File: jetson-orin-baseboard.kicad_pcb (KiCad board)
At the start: 8 copper layers, 110 x 55 mm, 223 parts, among them J1 ERF8-040-05.0-L-DV-K-TR, J2 46756-1001, J301 1-2199230-6, J302 2199230-6, J401 USB4105-GF-A, J402 WE_632723300011_alt_symbol, J501 WE_632723300011_alt_symbol, J601 5-2337992-8, J701 WE_68715014522, J702 WE_68715014522, J801 TC2050-IDC-NL, M1 M2_4222, M2 jetson-orin-nx/nano-module, M301 M2_2280, Q401 BSS138W-7-F, Q402 BSS138W-7-F, Q701 BSS138W-7-F, Q702 BSS138W-7-F, Q703 BSS138W-7-F, Q704 BSS138W-7-F, Q802 BSS138W-7-F, Q901 BSS138W-7-F, SW901 PCM12SMTR, U401 RB521S30T1G, U402 TPS65988, U403 W25Q80DVUXIE_TR, U405 FT230XQ-R, U406 TPS7B8133DRVR, U407 TUSB1046-DCI, U410 TPD4E05U06QDQARQ1, U412 TPD4E05U06QDQARQ1, U501 HD3SS3220, U602 ULS-12/5-D48N-C, U701 PCA9547BS, U702 AP22615, U703 AP22615, U704 NX3DV642, U705 NX3DV642, U706 AP22615, U707 AP22615, U803 PCAL6416AHF, U901 RB521S30T1G, U902 RB521S30T1G, U903 MP2386GG-P, U904 MP2386GG-P

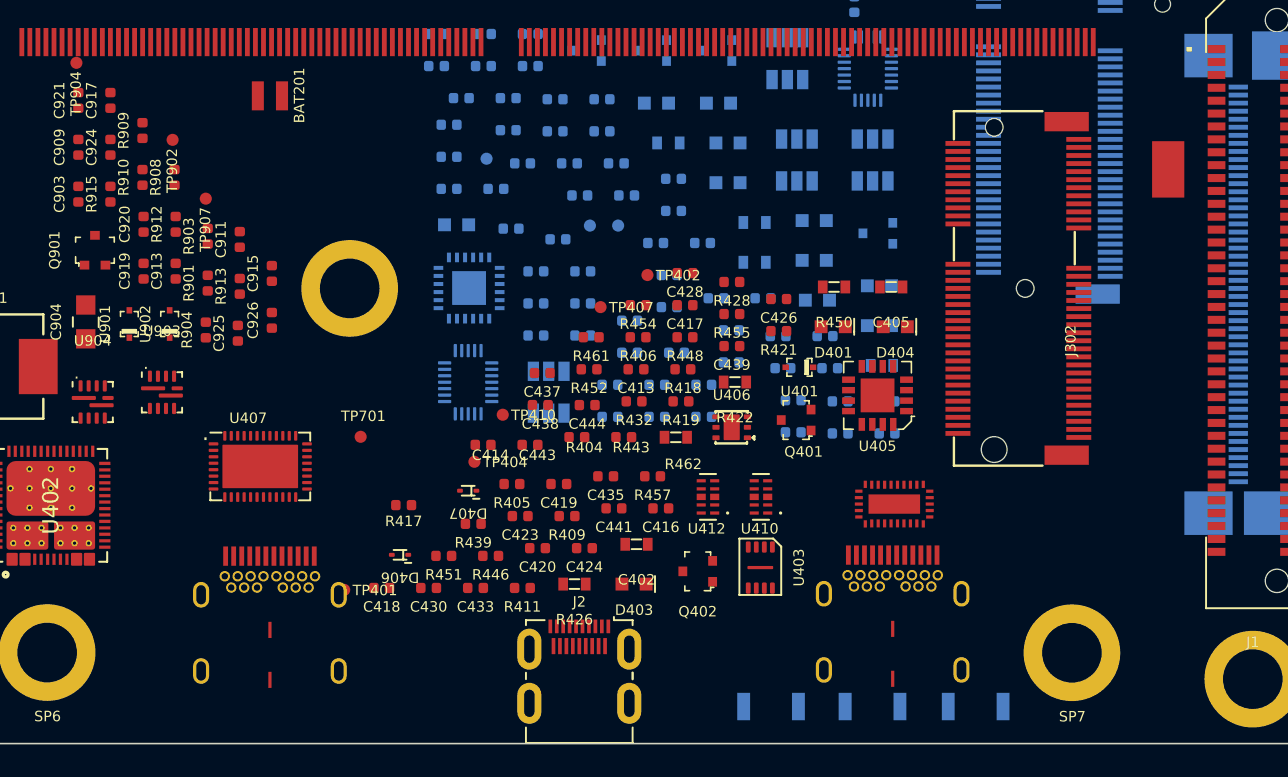
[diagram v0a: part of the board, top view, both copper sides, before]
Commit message: Update positions of the diodes
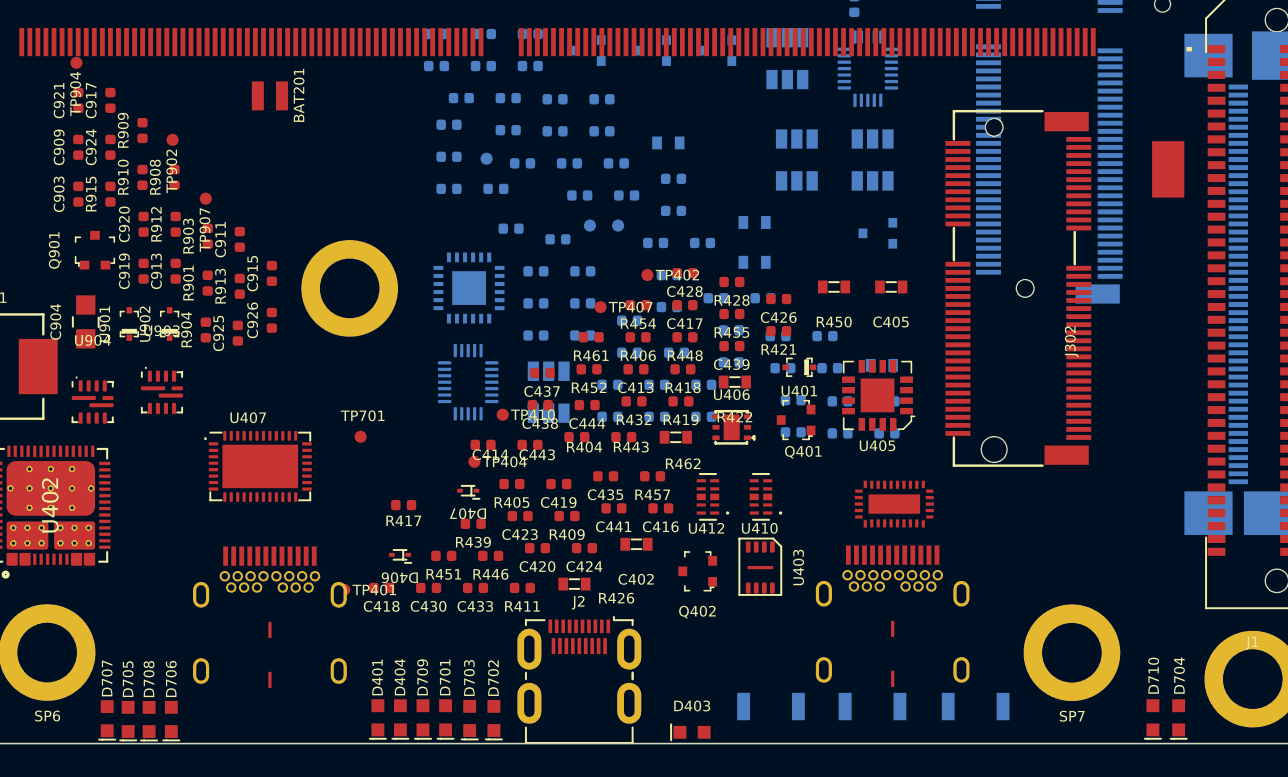
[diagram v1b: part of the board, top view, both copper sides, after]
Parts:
- D701, D702, D703, D704, D705, D706, D707, D708, D709, D710: moved to F.Cu
- moved D705 53.8 mm to (66.2, 123.5), turned to 90 degrees
- moved D706 50.3 mm to (68.9, 123.5), turned to 90 degrees
- moved D708 49.0 mm to (67.5, 123.5), turned to 90 degrees
- moved D701 41.7 mm to (85.9, 123.4), turned to 90 degrees
- moved D709 40.8 mm to (84.5, 123.4), turned to 90 degrees
- moved D703 39.2 mm to (87.4, 123.4), turned to 90 degrees
- moved D404 39.1 mm to (83.1, 123.4), turned to 90 degrees
- moved D707 37.5 mm to (64.9, 123.5), turned to 90 degrees
- moved D710 37.3 mm to (129.8, 123.4), turned to 90 degrees
- moved D401 37.3 mm to (81.7, 123.4), turned to 90 degrees
- moved D704 36.3 mm to (131.4, 123.4), turned to 90 degrees
- moved D702 36.3 mm to (88.9, 123.4), turned to 90 degrees
- moved D403 9.88 mm to (101.2, 124.3), turned to 0 degrees

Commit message: Import recently added components to PCB
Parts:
- removed the M1 at (124.8, 119.4)
- added A201: Jetson-Orin-9.2H-socket, antmicro-footprints:TE_2309413, F.Cu at (89.5, 77.4)
- added C1: C_1u_0402, antmicro-footprints:0402-cap, F.Cu at (-176.0, 142.6)
- added C10: C_100n_0402_50V, antmicro-footprints:0402-cap, F.Cu at (-168.9, 161.5)
- added C11: C_100n_0402, antmicro-footprints:0402-cap, F.Cu at (-151.4, 161.5)
- added C12: C_1u_0402, antmicro-footprints:0402-cap, F.Cu at (-168.2, 127.7)
- added C13: C_1u_0402, antmicro-footprints:0402-cap, F.Cu at (-185.8, 146.8)
- added C14: C_1u_0402, antmicro-footprints:0402-cap, F.Cu at (-163.5, 131.6)
- added C15: C_1u_0402, antmicro-footprints:0402-cap, F.Cu at (-180.0, 146.8)
- added C16: C_10u_25V_0603, antmicro-footprints:0603-cap, F.Cu at (-72.2, 116.4)
- added C17: C_10u_0402, antmicro-footprints:0402-cap, F.Cu at (-81.0, 130.0)
- added C18: C_100n_0402, antmicro-footprints:0402-cap, F.Cu at (-89.7, 92.7)
- added C19: C_100n_0402, antmicro-footprints:0402-cap, F.Cu at (-89.7, 90.8)
- added C2: C_100n_0402, antmicro-footprints:0402-cap, F.Cu at (-170.8, 136.6)
- added C20: C_100n_0402, antmicro-footprints:0402-cap, F.Cu at (-88.5, 88.8)
- added C201: C_22u_0805_25V, antmicro-footprints:0805-cap, F.Cu at (-276.4, 117.9)
- added C202: C_22u_0805_25V, antmicro-footprints:0805-cap, F.Cu at (-188.9, 86.8)
- added C203: C_22u_0805_25V, antmicro-footprints:0805-cap, F.Cu at (-264.6, 114.6)
- added C204: C_22u_0805_25V, antmicro-footprints:0805-cap, F.Cu at (-276.4, 120.8)
- added C205: C_100n_0402, antmicro-footprints:0402-cap, F.Cu at (-262.7, 117.0)
- added C21: C_100n_0402, antmicro-footprints:0402-cap, F.Cu at (-92.7, 94.7)
- added C22: C_100n_0402, antmicro-footprints:0402-cap, F.Cu at (-86.8, 92.7)
- added C23: C_100n_0402, antmicro-footprints:0402-cap, F.Cu at (-92.7, 98.7)
- added C24: C_100n_0402, antmicro-footprints:0402-cap, F.Cu at (-86.9, 94.7)
- added C25: C_100n_0402, antmicro-footprints:0402-cap, F.Cu at (-89.8, 96.7)
- added C26: C_100n_0402, antmicro-footprints:0402-cap, F.Cu at (-87.8, 86.3)
- added C27: C_100n_0402, antmicro-footprints:0402-cap, F.Cu at (-95.6, 93.9)
- added C28: C_100n_0402, antmicro-footprints:0402-cap, F.Cu at (-83.9, 92.3)
- added C29: C_100n_0402, antmicro-footprints:0402-cap, F.Cu at (-84.0, 94.7)
- added C3: C_100n_0402, antmicro-footprints:0402-cap, F.Cu at (-173.1, 134.6)
- added C30: C_100n_0402, antmicro-footprints:0402-cap, F.Cu at (-89.8, 94.7)
- added C301: C_10u_0603, antmicro-footprints:0603-cap, F.Cu at (-179.7, 96.6)
- added C302: C_10u_0603, antmicro-footprints:0603-cap, F.Cu at (-174.7, 89.0)
- added C303: C_10u_0603, antmicro-footprints:0603-cap, F.Cu at (-174.7, 91.5)
- added C304: C_10u_0603, antmicro-footprints:0603-cap, F.Cu at (-170.8, 86.5)
- added C305: C_100n_0402, antmicro-footprints:0402-cap, F.Cu at (-176.5, 98.4)
- added C306: C_100n_0402, antmicro-footprints:0402-cap, F.Cu at (-177.2, 105.3)
- added C307: C_100n_0402, antmicro-footprints:0402-cap, F.Cu at (-177.2, 103.3)
- added C308: C_100n_0402, antmicro-footprints:0402-cap, F.Cu at (-158.9, 88.3)
- added C309: C_100n_0402, antmicro-footprints:0402-cap, F.Cu at (-170.7, 99.2)
- added C31: C_100n_0402, antmicro-footprints:0402-cap, F.Cu at (-79.8, 88.3)
- added C310: C_100n_0402, antmicro-footprints:0402-cap, F.Cu at (-171.5, 93.2)
- added C311: C_100n_0402, antmicro-footprints:0402-cap, F.Cu at (-164.7, 86.3)
- added C312: C_100n_0402, antmicro-footprints:0402-cap, F.Cu at (-168.6, 92.3)
- added C313: C_100n_0402, antmicro-footprints:0402-cap, F.Cu at (-180.1, 103.3)
- added C318: C_100n_0402, antmicro-footprints:0402-cap, F.Cu at (-180.1, 101.3)
- added C32: C_100n_0402, antmicro-footprints:0402-cap, F.Cu at (-85.6, 88.3)
- added C323: C_10u_0603, antmicro-footprints:0603-cap, F.Cu at (-171.1, 89.0)
- added C324: C_10u_0603, antmicro-footprints:0603-cap, F.Cu at (-174.7, 93.9)
- added C33: C_100n_0402, antmicro-footprints:0402-cap, F.Cu at (-82.0, 86.3)
- added C34: C_100n_0402, antmicro-footprints:0402-cap, F.Cu at (-81.0, 90.3)
- added C35: C_100n_0402, antmicro-footprints:0402-cap, F.Cu at (-92.6, 90.8)
- added C36: C_100n_0402, antmicro-footprints:0402-cap, F.Cu at (-92.6, 92.7)
- added C37: C_100n_0402, antmicro-footprints:0402-cap, F.Cu at (-83.9, 90.3)
- added C38: C_4u7_0402, antmicro-footprints:0402-cap, F.Cu at (-98.5, 99.3)
- added C39: C_4u7_0402, antmicro-footprints:0402-cap, F.Cu at (-95.6, 97.9)
- added C4: C_100n_0402, antmicro-footprints:0402-cap, F.Cu at (-182.9, 146.8)
- added C401: C_100n_0402, antmicro-footprints:0402-cap, F.Cu at (-173.6, 179.2)
- added C412: C_100n_0402, antmicro-footprints:0402-cap, F.Cu at (-157.2, 161.5)
- added C415: C_100n_0402, antmicro-footprints:0402-cap, F.Cu at (-188.4, 181.0)
- added C421: C_100n_0402, antmicro-footprints:0402-cap, F.Cu at (-148.5, 159.5)
- added C422: C_100n_0402, antmicro-footprints:0402-cap, F.Cu at (-166.0, 161.5)
- added C425: C_100n_0402, antmicro-footprints:0402-cap, F.Cu at (-157.2, 159.5)
- added C427: C_100n_0402, antmicro-footprints:0402-cap, F.Cu at (-174.8, 173.2)
- added C429: C_100n_0402, antmicro-footprints:0402-cap, F.Cu at (-185.5, 181.4)
- added C431: C_100n_0402, antmicro-footprints:0402-cap, F.Cu at (-164.4, 163.5)
- added C432: C_100n_0402, antmicro-footprints:0402-cap, F.Cu at (-167.8, 176.4)
- added C434: C_10u_25V_0603, antmicro-footprints:0603-cap, F.Cu at (-187.2, 174.8)
- added C436: C_10u_0402, antmicro-footprints:0402-cap, F.Cu at (-168.9, 159.5)
- added C440: C_100n_0402, antmicro-footprints:0402-cap, F.Cu at (-164.4, 165.4)
- added C442: C_100n_0402, antmicro-footprints:0402-cap, F.Cu at (-180.7, 173.4)
- added C5: C_100n_0402, antmicro-footprints:0402-cap, F.Cu at (-167.9, 136.6)
- added C501: C_10u_0603, antmicro-footprints:0603-cap, F.Cu at (-277.0, 201.0)
- added C503: C_100n_0402, antmicro-footprints:0402-cap, F.Cu at (-257.1, 187.3)
- added C505: C_100n_0402, antmicro-footprints:0402-cap, F.Cu at (-273.5, 198.3)
- added C507: C_100n_0402, antmicro-footprints:0402-cap, F.Cu at (-272.6, 195.8)
- added C508: C_100n_0402, antmicro-footprints:0402-cap, F.Cu at (-270.6, 197.8)
- added C511: C_100n_0402, antmicro-footprints:0402-cap, F.Cu at (-265.0, 199.8)
- added C512: C_100n_0402, antmicro-footprints:0402-cap, F.Cu at (-261.8, 197.3)
- added C515: C_100n_0402, antmicro-footprints:0402-cap, F.Cu at (-269.7, 195.8)
- added C517: C_10u_0603, antmicro-footprints:0603-cap, F.Cu at (-272.3, 191.6)
- added C519: C_100n_0402, antmicro-footprints:0402-cap, F.Cu at (-267.9, 199.8)
- added C6: C_100n_0402, antmicro-footprints:0402-cap, F.Cu at (-176.0, 140.6)
- added C601: C_100n_0805_100V, antmicro-footprints:0805-cap, F.Cu at (-254.0, 157.9)
- added C602: C_10n_0402, antmicro-footprints:0402-cap, F.Cu at (-251.4, 160.4)
- added C604: C_22u_2220_100V, antmicro-footprints:2220-cap, F.Cu at (-274.6, 164.4)
- added C607: C_100n_0402, antmicro-footprints:0402-cap, F.Cu at (-268.9, 175.1)
- added C608: C_47u_16V_1206, antmicro-footprints:1206-cap, F.Cu at (-275.4, 169.6)
- added C609: C_47u_16V_1206, antmicro-footprints:1206-cap, F.Cu at (-267.0, 165.5)
- added C610: C_100n_0402_16V, antmicro-footprints:0402-cap, F.Cu at (-257.4, 166.2)
- added C611: C_100n_0402, antmicro-footprints:0402-cap, F.Cu at (-270.9, 180.1)
- added C7: C_100n_0402, antmicro-footprints:0402-cap, F.Cu at (-169.3, 132.6)
- added C8: C_100n_0402_50V, antmicro-footprints:0402-cap, F.Cu at (-183.6, 173.4)
- added C804: C_100n_0402, antmicro-footprints:0402-cap, F.Cu at (-170.2, 134.6)
- added C810: C_100n_0402, antmicro-footprints:0402-cap, F.Cu at (-183.5, 150.8)
- added C812: C_100n_0402, antmicro-footprints:0402-cap, F.Cu at (-186.4, 151.0)
- added C9: C_100n_0402, antmicro-footprints:0402-cap, F.Cu at (-178.2, 175.4)
- added C901: C_22u_0805_25V, antmicro-footprints:0805-cap, F.Cu at (-90.2, 125.2)
- added C902: C_22u_0805_25V, antmicro-footprints:0805-cap, F.Cu at (-85.1, 116.6)
- added C905: C_22u_0805_25V, antmicro-footprints:0805-cap, F.Cu at (-81.0, 119.5)
- added C906: C_22u_0805_25V, antmicro-footprints:0805-cap, F.Cu at (-80.3, 116.6)
- added C907: C_22u_0805_25V, antmicro-footprints:0805-cap, F.Cu at (-100.5, 140.0)
- added C908: C_100n_0402_50V, antmicro-footprints:0402-cap, F.Cu at (-84.9, 133.3)
- added C910: C_1u_0402, antmicro-footprints:0402-cap, F.Cu at (-70.6, 120.6)
- added C912: C_10u_0402, antmicro-footprints:0402-cap, F.Cu at (-63.8, 118.1)
- added C914: C_220n_0402, antmicro-footprints:0402-cap, F.Cu at (-97.6, 142.7)
- added C916: C_33p_0402, antmicro-footprints:0402-cap, F.Cu at (-82.2, 126.0)
- added C918: C_22u_0402, antmicro-footprints:0402-cap, F.Cu at (-81.0, 128.0)
- added C922: C_100n_0402, antmicro-footprints:0402-cap, F.Cu at (-84.6, 131.3)
- added C923: C_22u_0402, antmicro-footprints:0402-cap, F.Cu at (-87.1, 139.2)
- added C927: C_1u_0402, antmicro-footprints:0402-cap, F.Cu at (-89.1, 137.2)
- added D1: 1N4148WS, Diode_SMD:D_SOD-323, F.Cu at (-97.8, 86.8)
- added D301: KP-1608CGCK, antmicro-footprints:LED_0603, F.Cu at (-174.5, 86.5)
- added D402: LTST-C190GKT, antmicro-footprints:LED_0603, F.Cu at (-190.6, 172.3)
- added D405: LTST-C190GKT, antmicro-footprints:LED_0603, F.Cu at (-195.3, 181.4)
- added D408: LTST-C190GKT, antmicro-footprints:LED_0603, F.Cu at (-181.9, 163.8)
- added D501: ESD9X5.0ST5G, antmicro-footprints:SOD-923, F.Cu at (-257.6, 193.3)
- added D503: LTST-C190GKT, antmicro-footprints:LED_0603, F.Cu at (-276.9, 198.5)
- added D601: CD-MMBL110S, antmicro-footprints:DFN3538, F.Cu at (-258.9, 159.6)
- added D602: CD-MMBL110S, antmicro-footprints:DFN3538, F.Cu at (-276.4, 174.4)
- added D603: PTVS58VS1UR,115, antmicro-footprints:SOD-123F, F.Cu at (-269.4, 169.6)
- added D604: KP-1608CGCK, antmicro-footprints:LED_0603, F.Cu at (-276.9, 178.7)
- added D801: LTST-C190GKT, antmicro-footprints:LED_0603, F.Cu at (-189.2, 146.7)
- added D802: LTST-C190GKT, antmicro-footprints:LED_0603, F.Cu at (-182.3, 140.6)
- added FB1: BLM18SG121TN1D, antmicro-footprints:0603-res, F.Cu at (-91.1, 86.5)
- added FB201: 74279221100, antmicro-footprints:1206-res, F.Cu at (-275.4, 114.8)
- added FB601: BLM21PG221SN1D, antmicro-footprints:0805-res, F.Cu at (-261.2, 165.3)
- added FB602: BLM21PG221SN1D, antmicro-footprints:0805-res, F.Cu at (-271.5, 172.7)
- added IC601: ACPL-217-500E, antmicro-footprints:SOIC127P700X242-4N, F.Cu at (-273.9, 158.7)
- added IC901: TPS7A0518PDBVT, antmicro-footprints:SOT-23-5, F.Cu at (-94.9, 125.9)
- added J3: PJ-102A, antmicro-footprints:Barrel_Jack_5.5mmODx2.1mmID_PJ-102A, F.Cu at (-96.8, 159.0)
- added J803: 533980471, antmicro-footprints:Molex_PicoBlade_53398-0471_1x04-1MP_P1.25mm_Vertical, F.Cu at (-190.7, 137.4)
- added Q1: BCM857BS-7-F, antmicro-footprints:SOT-363, F.Cu at (-81.5, 123.0)
- added Q2: BCM857BS-7-F, antmicro-footprints:SOT-363, F.Cu at (-75.9, 117.1)
- added Q3: SSM3J332R, antmicro-footprints:SOT-23-3, F.Cu at (-97.0, 136.1)
- added Q4: SSM3J332R, antmicro-footprints:SOT-23-3, F.Cu at (-92.3, 131.0)
- added Q5: BSS138APW, antmicro-footprints:SC70-3, F.Cu at (-101.3, 170.6)
- added Q501: BSS138W-7-F, antmicro-footprints:SOT-323, F.Cu at (-272.9, 188.3)
- added Q801: BSS138W-7-F, antmicro-footprints:SOT-323, F.Cu at (-195.2, 148.3)
- added Q803: BSS138W-7-F, antmicro-footprints:SOT-323, F.Cu at (-175.2, 128.7)
- added Q902: BSS138W-7-F, antmicro-footprints:SOT-323, F.Cu at (-85.7, 125.7)
- added Q903: BSS138W-7-F, antmicro-footprints:SOT-323, F.Cu at (-92.6, 135.5)
- added R1: R_0R_0402, antmicro-footprints:0402-res, F.Cu at (-180.1, 105.3)
- added R10: R_0R_0402, antmicro-footprints:0402-res, F.Cu at (-165.3, 129.7)
- added R11: R_0R_0402, antmicro-footprints:0402-res, F.Cu at (-173.1, 140.6)
- added R12: R_0R_0402, antmicro-footprints:0402-res, F.Cu at (-185.8, 148.8)
- added R13: R_0R_0402, antmicro-footprints:0402-res, F.Cu at (-180.1, 107.3)
- added R14: R_0R_0402, antmicro-footprints:0402-res, F.Cu at (-170.7, 97.2)
- added R15: R_0R_0402, antmicro-footprints:0402-res, F.Cu at (-164.9, 94.3)
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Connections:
- net /Ethernet/VIN_POE renamed POE_OUTPUT
- net /USB Debug, DP/USBC3_D_P renamed Net-(J401-PadA6)
- C917 pad 1: +3V3 -> Net-(C917-Pad1)
- C919 pad 1: +3V3 -> Net-(C917-Pad1)
- C920 pad 1: +5V -> Net-(C916-Pad1)
- C921 pad 1: +3V3 -> Net-(C917-Pad1)
- C924 pad 1: +3V3 -> Net-(C917-Pad1)
- J1 pad 31: GND -> GPIO01
- J1 pad 33: /Peripherals/EXT_GPIO2 -> GPIO07
- J1 pad 34: GND -> PCIE_WAKE_EXT
- J1 pad 35: /Peripherals/EXT_GPIO3 -> GPIO09
- J1 pad 36: /Peripherals/EXT_GPIO0 -> GPIO13
- J1 pad 38: /Peripherals/EXT_GPIO1 -> GND
- J1 pad 39: GPIO12 -> GPIO10
- J1 pad 40: GND -> GPIO12
- J1 pad 41: GPIO13 -> UART0_TXD
- J1 pad 42: GPIO01 -> GPIO11
- J1 pad 43: GPIO09 -> UART0_RXD
- J1 pad 44: GPIO07 -> GPIO00
- J1 pad 45: GPIO10 -> I2S0_SDIN
- J1 pad 46: I2C2_SDA -> I2S0_SCLK
- J1 pad 48: I2C2_SCL -> I2S0_SDOUT
- J2 pad 1: unconnected-(J2-Pad1) -> /HDMI/HDMI_HPD_5V
- J2 pad 10: unconnected-(J2-Pad10) -> GND
- J2 pad 11: unconnected-(J2-Pad11) -> /HDMI/HDMI_D0_CONN_N
- J2 pad 12: unconnected-(J2-Pad12) -> /HDMI/HDMI_CLK_CONN_P
- J2 pad 13: unconnected-(J2-Pad13) -> GND
- J2 pad 14: unconnected-(J2-Pad14) -> /HDMI/HDMI_CLK_CONN_N
- J2 pad 15: unconnected-(J2-Pad15) -> /HDMI/HDMI_CEC_5V
- J2 pad 16: unconnected-(J2-Pad16) -> GND
- J2 pad 17: unconnected-(J2-Pad17) -> /HDMI/HDMI_SCL_5V
- J2 pad 18: unconnected-(J2-Pad18) -> /HDMI/HDMI_SDA_5V
- J2 pad 19: unconnected-(J2-Pad19) -> /HDMI/5V_HDMI
- J2 pad 3: unconnected-(J2-Pad3) -> /HDMI/HDMI_D2_CONN_P
- J2 pad 4: unconnected-(J2-Pad4) -> GND
- J2 pad 5: unconnected-(J2-Pad5) -> /HDMI/HDMI_D2_CONN_N
- J2 pad 6: unconnected-(J2-Pad6) -> /HDMI/HDMI_D1_CONN_P
- J2 pad 7: unconnected-(J2-Pad7) -> GND
- J2 pad 8: unconnected-(J2-Pad8) -> /HDMI/HDMI_D1_CONN_N
- J2 pad 9: unconnected-(J2-Pad9) -> /HDMI/HDMI_D0_CONN_P
- J2 pad SH: unconnected-(J2-PadSH) -> GND
- J302 pad 10: unconnected-(J302-Pad10) -> Net-(J302-Pad10)
- J302 pad 12: unconnected-(J302-Pad12) -> Net-(J302-Pad12)
- J302 pad 14: unconnected-(J302-Pad14) -> Net-(J302-Pad14)
- J302 pad 22: unconnected-(J302-Pad22) -> Net-(J302-Pad22)
- J302 pad 32: unconnected-(J302-Pad32) -> Net-(J302-Pad32)
- J302 pad 34: unconnected-(J302-Pad34) -> Net-(J302-Pad34)
- J302 pad 36: unconnected-(J302-Pad36) -> Net-(J302-Pad36)
- J302 pad 56: PCIE1_DISABLE -> Net-(J302-Pad56)
- J302 pad 58: unconnected-(J302-Pad58) -> Net-(J302-Pad58)
- J302 pad 60: unconnected-(J302-Pad60) -> Net-(J302-Pad60)
- J302 pad 8: unconnected-(J302-Pad8) -> Net-(J302-Pad8)
- J801 pad 1: FTDI_TXD -> DEBUG_TXD
- J801 pad 2: FTDI_RXD -> DEBUG_RXD
- L901 pad 2: +5V -> Net-(C916-Pad1)
- L902 pad 2: +3V3 -> Net-(C917-Pad1)
- R909 pad 2: +5V -> Net-(C916-Pad1)
- TP907 pad 1: +1V8 -> Net-(C927-Pad1)
- U402 pad 1: unconnected-(U402-Pad1) -> USBPD1_HV
- U402 pad 11: unconnected-(U402-Pad11) -> USBPD2_HV
- U402 pad 48: unconnected-(U402-Pad48) -> /USB Debug, DP/USBC3_5V_PEN
- U402 pad 49: unconnected-(U402-Pad49) -> /USB Debug, DP/USBC0_5V_PEN
- U803 pad 7: /Peripherals/GPIOEX_P0_6 -> unconnected-(U803-Pad7)

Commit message: Import annotation and recent changes to PCB, unify reference designators size
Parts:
- removed BAT201: MS621FE-FL11E, antmicro-footprints:MS621FE-FL11E
- removed C201, C202, C203, C204, C901, C902, C904, C905, C906, C907: C_22u_0805_25V, antmicro-footprints:0805-cap
- removed C205, C305, C306, C307, C308, C309, C310, C311, C312, C313, C318, C401, C412, C413, C414, C415, C416, C417, C418, C419, C420, C421, C422, C423, C424, C425, C426, C427, C428, C429, C430, C431, C432, C433, C439, C440, C441, C442, C503, C505, C507, C508, C511, C512, C515, C519, C607, C611, C701, C702, C703, C704, C705, C706, C707, C804, C810, C812, C915, C922, C925: C_100n_0402, antmicro-footprints:0402-cap
- removed C301, C302, C303, C304, C323, C324, C402, C405, C501, C517: C_10u_0603, antmicro-footprints:0603-cap
- removed C434: C_10u_25V_0603, antmicro-footprints:0603-cap
- removed C435, C436, C437, C438, C903, C912: C_10u_0402, antmicro-footprints:0402-cap
- removed C443, C444, C908, C909: C_100n_0402_50V, antmicro-footprints:0402-cap
- removed C601: C_100n_0805_100V, antmicro-footprints:0805-cap
- removed C602: C_10n_0402, antmicro-footprints:0402-cap
- removed C604: C_22u_2220_100V, antmicro-footprints:2220-cap
- removed C608, C609: C_47u_16V_1206, antmicro-footprints:1206-cap
- removed C610: C_100n_0402_16V, antmicro-footprints:0402-cap
- removed C708, C709, C710, C711, C910, C911, C927: C_1u_0402, antmicro-footprints:0402-cap
- removed C913, C914: C_220n_0402, antmicro-footprints:0402-cap
- removed C916, C917: C_33p_0402, antmicro-footprints:0402-cap
- removed C918, C919, C920, C921, C923, C924: C_22u_0402, antmicro-footprints:0402-cap
- removed C926: C_2u2_0402, antmicro-footprints:0402-cap
- removed D301, D604: KP-1608CGCK, antmicro-footprints:LED_0603
- removed D401, D402, D403, D404, D405, D408, D503, D701, D702, D703, D704, D705, D706, D707, D708, D709, D710, D801, D802: LTST-C190GKT, antmicro-footprints:LED_0603
- removed D406, D407: DF2S30FS, antmicro-footprints:SOD-923
- removed D501: ESD9X5.0ST5G, antmicro-footprints:SOD-923
- removed D601, D602: CD-MMBL110S, antmicro-footprints:DFN3538
- removed D603: PTVS58VS1UR,115, antmicro-footprints:SOD-123F
- removed FB201: 74279221100, antmicro-footprints:1206-res
- removed FB601, FB602: BLM21PG221SN1D, antmicro-footprints:0805-res
- removed IC601: ACPL-217-500E, antmicro-footprints:SOIC127P700X242-4N
- removed IC901: TPS7A0518PDBVT, antmicro-footprints:SOT-23-5
- removed the J3 at (-96.8, 159.0)
- removed J801: TC2050-IDC-NL, antmicro-footprints:TC2050-IDC-NL_2x05_Vertical
- removed J803: 533980471, antmicro-footprints:Molex_PicoBlade_53398-0471_1x04-1MP_P1.25mm_Vertical
- removed L901, L902: IHLP2525CZER2R2M01, antmicro-footprints:IHLP2525CZER
- removed Q401, Q402, Q501, Q701, Q702, Q703, Q704, Q801, Q802, Q803, Q901, Q902, Q903: BSS138W-7-F, antmicro-footprints:SOT-323
- removed R301, R302, R303, R312, R313, R402, R404, R428, R505, R507, R509, R529, R545, R547, R549, R551, R608, R609, R612, R704, R709, R710, R725, R726, R823, R826, R827, R828, R913: R_10k_0402, antmicro-footprints:0402-res
- removed R304, R305, R306, R308, R309, R316, R401, R406, R407, R408, R409, R410, R411, R417, R418, R419, R420, R421, R424, R425, R429, R430, R431, R432, R433, R434, R451, R452, R453, R454, R455, R456, R457, R458, R503, R504, R510, R511, R512, R513, R514, R515, R516, R517, R532, R533, R534, R535, R536, R537, R705, R706, R707, R708, R713, R716, R721, R723, R724, R741, R742, R743, R744, R749, R750, R751, R752, R802, R803, R804, R806, R811, R812, R813, R814, R815, R816, R904, R905, R914, R916: R_0R_0402, antmicro-footprints:0402-res
- removed R307: R_330R_0603, antmicro-footprints:0603-res
- removed R403, R405, R435, R461, R702, R722, R734, R738, R808, R818, R901, R907, R908: R_100k_0402, antmicro-footprints:0402-res
- removed R422, R423, R426, R427, R450, R462, R736, R747: R_200R_0603, antmicro-footprints:0603-res
- removed R436, R437, R438, R439, R440, R441, R442, R443, R444, R445, R446, R447, R448, R449, R902: R_1k_0402, antmicro-footprints:0402-res
- removed R459, R460: R_2M0_0402, antmicro-footprints:0402-res
- removed R527, R903, R906, R915: R_200k_0402, antmicro-footprints:0402-res
- removed R531: R_887k_0402, antmicro-footprints:0402-res
- removed R553, R701, R703, R711, R712, R714, R715, R719, R720: R_2k2_0402, antmicro-footprints:0402-res
- removed R555, R739, R748: R_470R_0603, antmicro-footprints:0603-res
- removed R601: R_1k3_0603, antmicro-footprints:0603-res
- removed R602: R_49k9_0402, antmicro-footprints:0402-res
- removed R603, R607, R616: R_0R_0603, antmicro-footprints:0603-res
- removed R604: R_63R4_0603, antmicro-footprints:0603-res
- removed R605: R_1k2_0402, antmicro-footprints:0402-res
- removed R606: R_24k9_0402, antmicro-footprints:0402-res
- removed R610, R611: R_220R_0402, antmicro-footprints:0402-res
- removed R613: R_32k4_0402, antmicro-footprints:0402-res
- removed R614, R615: R_1k_0603, antmicro-footprints:0603-res
- removed R617, R733, R735, R737, R740, R745, R746, R809, R819: R_200R_0402, antmicro-footprints:0402-res
- removed R717, R718, R727, R728: R_4k7_0402, antmicro-footprints:0402-res
- removed R729, R730, R731, R732: R_49R9_0402, antmicro-footprints:0402-res
- removed R807: R_10k2_0402, antmicro-footprints:0402-res
- removed R909, R911: R_40k2_1%_0402, antmicro-footprints:0402-res
- removed R910: R_5k49_1%_0402, antmicro-footprints:0402-res
- removed R912: R_8k87_1%_0402, antmicro-footprints:0402-res
- removed S201, S801, S802, S901, S902: B3U-3000PM, antmicro-footprints:B3U-3000P
- removed TP201, TP202, TP401, TP402, TP403, TP404, TP405, TP406, TP407, TP408, TP409, TP410, TP411, TP412, TP413, TP501, TP505, TP506, TP507, TP701, TP702, TP703, TP704, TP901, TP902, TP903, TP904, TP905, TP907: TP_SMD_0_75MM, antmicro-footprints:Testpoint_smd_0_75mm
- removed U201: 74LVC2G17GV, antmicro-footprints:SC-74
- removed U301, U302: 74LVC2G07GV, antmicro-footprints:SC-74
- removed U401, U901, U902: RB521S30T1G, antmicro-footprints:SOD-523
- removed U402: TPS65988, antmicro-footprints:IC_TPS65987DDHRSHR
- removed U403: W25Q80DVUXIE_TR, antmicro-footprints:USON-8_2x3mm_P0.5mm
- removed U405: FT230XQ-R, antmicro-footprints:WQFN-16-1EP_4x4mm
- removed U406: TPS7B8133DRVR, antmicro-footprints:WSON6_TI_2x2mm
- removed U407: TUSB1046-DCI, antmicro-footprints:WQFN-40_1EP_6x3mm_Pitch0.4mm_EP4.7x2.7mm
- removed U408, U409, U410, U411, U412, U505, U507, U509: TPD4E05U06QDQARQ1, antmicro-footprints:USON-10_2.5x1.0mm_P0.5mm
- removed U501: HD3SS3220, antmicro-footprints:RNH0030A
- removed U503, U702, U703, U706, U707: AP22615, antmicro-footprints:TSOT23-6
- removed U601: TPS2372-3RGWR, antmicro-footprints:Texas_RGW0020B
- removed U701: PCA9547BS, antmicro-footprints:VQFN-24
- removed U803: PCAL6416AHF, antmicro-footprints:QFN-24-1EP_4x4mm
- removed U807: 74LVC1T45GM, antmicro-footprints:SOT-886
- removed U903, U904: MP2386GG-P, antmicro-footprints:QFN-11_2x2mm_P0.5mm
- removed U905: 74LVC2G14GV, antmicro-footprints:SOT23-6L
- removed U906: 74LVC1G175GV, antmicro-footprints:SOT-23-6
- added BAT1: MS621FE-FL11E, antmicro-footprints:MS621FE-FL11E, F.Cu at (-64.5, 134.8)
- added C100: C_100n_0402, antmicro-footprints:0402-cap, F.Cu at (-67.5, 72.7)
- added C101: C_100n_0402, antmicro-footprints:0402-cap, F.Cu at (-64.6, 70.7)
- added C102: C_100n_0402, antmicro-footprints:0402-cap, F.Cu at (-86.4, 117.5)
- added C103: C_100n_0402, antmicro-footprints:0402-cap, F.Cu at (-80.1, 114.7)
- added C104: C_100n_0402, antmicro-footprints:0402-cap, F.Cu at (-86.9, 121.4)
- added C105: C_1u_0402, antmicro-footprints:0402-cap, F.Cu at (-72.7, 100.7)
- added C106: C_1u_0402, antmicro-footprints:0402-cap, F.Cu at (-69.8, 100.7)
- added C107: C_1u_0402, antmicro-footprints:0402-cap, F.Cu at (-77.2, 114.7)
- added C108: C_100n_0402, antmicro-footprints:0402-cap, F.Cu at (-69.8, 104.7)
- added C109: C_100n_0402, antmicro-footprints:0402-cap, F.Cu at (-83.0, 115.4)
- added C110: C_100n_0402, antmicro-footprints:0402-cap, F.Cu at (-72.7, 106.6)
- added C111: C_100n_0402, antmicro-footprints:0402-cap, F.Cu at (-64.0, 102.7)
- added C112: C_100n_0402, antmicro-footprints:0402-cap, F.Cu at (-66.9, 100.7)
- added C113: C_100n_0402, antmicro-footprints:0402-cap, F.Cu at (-69.8, 102.7)
- added C114: C_1u_0402, antmicro-footprints:0402-cap, F.Cu at (-69.8, 108.6)
- added C115: C_1u_0402, antmicro-footprints:0402-cap, F.Cu at (-72.7, 102.7)
- added C116: C_10u_0402, antmicro-footprints:0402-cap, F.Cu at (-108.2, 70.7)
- added C117: C_10u_0402, antmicro-footprints:0402-cap, F.Cu at (-106.4, 68.8)
- added C118: C_100n_0402, antmicro-footprints:0402-cap, F.Cu at (-132.5, 87.9)
- added C119: C_100n_0402, antmicro-footprints:0402-cap, F.Cu at (-118.3, 73.3)
- added C120: C_22u_0805_25V, antmicro-footprints:0805-cap, F.Cu at (-146.9, 86.8)
- added C121: C_22u_0805_25V, antmicro-footprints:0805-cap, F.Cu at (-123.6, 67.2)
- added C122: C_22u_0805_25V, antmicro-footprints:0805-cap, F.Cu at (-156.6, 94.9)
- added C123: C_22u_0805_25V, antmicro-footprints:0805-cap, F.Cu at (-143.8, 90.6)
- added C124: C_100n_0402, antmicro-footprints:0402-cap, F.Cu at (-131.6, 93.8)
- added C125: C_22u_0805_25V, antmicro-footprints:0805-cap, F.Cu at (-128.5, 67.2)
- added C126: C_22u_0805_25V, antmicro-footprints:0805-cap, F.Cu at (-124.3, 70.1)
- added C127: C_100n_0402_50V, antmicro-footprints:0402-cap, F.Cu at (-133.2, 89.8)
- added C128: C_100n_0402_50V, antmicro-footprints:0402-cap, F.Cu at (-137.4, 94.1)
- added C129: C_1u_0402, antmicro-footprints:0402-cap, F.Cu at (-134.5, 93.8)
- added C130: C_1u_0402, antmicro-footprints:0402-cap, F.Cu at (-136.1, 89.2)
- added C131: C_2u2_0402, antmicro-footprints:0402-cap, F.Cu at (-129.6, 88.5)
- added C132: C_220n_0402, antmicro-footprints:0402-cap, F.Cu at (-124.3, 81.1)
- added C133: C_220n_0402, antmicro-footprints:0402-cap, F.Cu at (-122.8, 76.6)
- added C134: C_10u_25V_0603, antmicro-footprints:0603-cap, F.Cu at (-120.1, 71.1)
- added C135: C_33p_0402, antmicro-footprints:0402-cap, F.Cu at (-121.2, 73.3)
- added C136: C_33p_0402, antmicro-footprints:0402-cap, F.Cu at (-106.4, 66.8)
- added C137: C_10u_0402, antmicro-footprints:0402-cap, F.Cu at (-115.4, 72.8)
- added C138: C_22u_0402, antmicro-footprints:0402-cap, F.Cu at (-132.5, 85.9)
- added C139: C_22u_0402, antmicro-footprints:0402-cap, F.Cu at (-112.3, 68.8)
- added C140: C_22u_0402, antmicro-footprints:0402-cap, F.Cu at (-136.1, 91.2)
- added C141: C_22u_0402, antmicro-footprints:0402-cap, F.Cu at (-126.6, 89.1)
- added C142: C_1u_0402, antmicro-footprints:0402-cap, F.Cu at (-119.9, 77.3)
- added C143: C_22u_0402, antmicro-footprints:0402-cap, F.Cu at (-130.3, 90.5)
- added C144: C_22u_0402, antmicro-footprints:0402-cap, F.Cu at (-121.4, 79.3)
- added C145: C_100n_0402, antmicro-footprints:0402-cap, F.Cu at (-40.2, 94.8)
- added C146: C_100n_0402, antmicro-footprints:0402-cap, F.Cu at (-52.6, 104.4)
- added C147: C_100n_0402, antmicro-footprints:0402-cap, F.Cu at (-50.4, 102.4)
- added C148: C_100n_0402, antmicro-footprints:0402-cap, F.Cu at (-43.1, 96.7)
- added C149: C_100n_0402, antmicro-footprints:0402-cap, F.Cu at (-37.3, 94.8)
- added C150: C_100n_0402, antmicro-footprints:0402-cap, F.Cu at (-46.8, 104.7)
- added C151: C_100n_0402, antmicro-footprints:0402-cap, F.Cu at (-43.9, 102.7)
- added C152: C_100n_0402, antmicro-footprints:0402-cap, F.Cu at (-37.3, 96.7)
- added C153: C_100n_0402, antmicro-footprints:0402-cap, F.Cu at (-37.4, 98.7)
- added C154: C_100n_0402, antmicro-footprints:0402-cap, F.Cu at (-53.3, 102.4)
- added C155: C_100n_0402, antmicro-footprints:0402-cap, F.Cu at (-34.4, 94.8)
- added C156: C_100n_0402, antmicro-footprints:0402-cap, F.Cu at (-37.8, 100.7)
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- renumbered A201 to A1, C603 to C79, C605 to C81, C606 to C82, J302 to J1, J1 to J11, J2 to J13, J301 to J2, J401 to J3, J402 to J4, J501 to J5, J601 to J6, J701 to J7, J702 to J8, M2 to M1, M1 to M2, M301 to M3, SP2 to SP1, SP3 to SP2, SP4 to SP3, SP5 to SP4, SP6 to SP5, SP7 to SP6, SP1 to SP7, SP301 to SP8, SW901 to SW1, U602 to U23, U704 to U27, U705 to U28
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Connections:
- net Net-(J401-PadA6) renamed /USB Debug, DP/USBC3_D_P
- A1 pad 101: Net-(A201-Pad101) -> UART0_RXD
- A1 pad 103: unconnected-(A201-Pad103) -> UART0_RTS
- A1 pad 105: unconnected-(A201-Pad105) -> UART0_CTS
- A1 pad 114: Net-(A201-Pad114) -> Net-(A1-Pad114)
- A1 pad 116: unconnected-(A201-Pad116) -> Net-(A1-Pad116)
- A1 pad 120: Net-(A201-Pad120) -> Net-(A1-Pad120)
- A1 pad 122: unconnected-(A201-Pad122) -> Net-(A1-Pad122)
- A1 pad 124: Net-(A201-Pad124) -> Net-(A1-Pad124)
- A1 pad 185: Net-(A201-Pad185) -> Net-(A1-Pad185)
- A1 pad 187: Net-(A201-Pad187) -> Net-(A1-Pad187)
- A1 pad 189: Net-(A201-Pad189) -> Net-(A1-Pad189)
- A1 pad 191: Net-(A201-Pad191) -> Net-(A1-Pad191)
- A1 pad 207: UART1_RTS -> unconnected-(A1-Pad207)
- A1 pad 209: UART1_CTS -> unconnected-(A1-Pad209)
- A1 pad 210: CLK_32K_OUT -> /SoM/CLK_32K_OUT
- A1 pad 217: Net-(A201-Pad217) -> /SoM/MODULE_ID
- A1 pad 218: GPIO12 -> Net-(A1-Pad218)
- A1 pad 228: GPIO13 -> Net-(A1-Pad228)
- A1 pad 99: Net-(A201-Pad99) -> UART0_TXD
- C1 pad 1: /Peripherals/5V_CONN -> /SoM/SoM_VDD_IN
- C10 pad 1: USBPD2_HV -> PCIE1_TX0_N
- C10 pad 2: GND -> /M.2/C_PCIE1_TX0_N
- C11 pad 1: +5V -> +3V3
- C12 pad 1: /Peripherals/3V3_CONN -> +3V3
- C13 pad 1: /Peripherals/1V8_CONN -> PCIE0_TX0_P
- C13 pad 2: GND -> /M.2/C_PCIE0_TX0_P
- C14 pad 1: /Peripherals/3V3_STDB_CONN -> PCIE0_TX1_P
- C14 pad 2: GND -> /M.2/C_PCIE0_TX1_P
- C15 pad 1: /Peripherals/12V_CONN -> PCIE0_TX2_P
- C15 pad 2: GND -> /M.2/C_PCIE0_TX2_P
- C16 pad 1: VCC -> PCIE0_TX3_P
- C16 pad 2: GND -> /M.2/C_PCIE0_TX3_P
- C17 pad 1: Net-(C17-Pad1) -> PCIE0_TX0_N
- C17 pad 2: GND -> /M.2/C_PCIE0_TX0_N
- C18 pad 1: /HDMI/HDMI_D2_N -> PCIE0_TX1_N
- C18 pad 2: DP1_TXD0_HDMI_TX2_N -> /M.2/C_PCIE0_TX1_N
- C19 pad 1: /HDMI/HDMI_D1_N -> PCIE0_TX2_N
- C19 pad 2: DP1_TXD1_HDMI_TX1_N -> /M.2/C_PCIE0_TX2_N
- C2 pad 1: PCIE2_TX0_N -> /SoM/SoM_VDD_IN
- C2 pad 2: /Peripherals/PCIE2_TX0_CONN_N -> GND
- C20 pad 1: /HDMI/HDMI_D0_N -> PCIE0_TX3_N
- C20 pad 2: DP1_TXD2_HDMI_TX0_N -> /M.2/C_PCIE0_TX3_N
- C21 pad 1: /HDMI/HDMI_CLK_N -> +3V3
- C21 pad 2: DP1_TXD3_HDMI_TXC_N -> GND
- C22 pad 1: DP1_TXD0_N -> +3V3
- C22 pad 2: DP1_TXD0_HDMI_TX2_N -> GND
- C23 pad 1: DP1_TXD1_N -> +3V3
- C23 pad 2: DP1_TXD1_HDMI_TX1_N -> GND
- C24 pad 1: DP1_TXD2_N -> +3V3
- C24 pad 2: DP1_TXD2_HDMI_TX0_N -> GND
- C25 pad 1: DP1_TXD3_N -> +3V3
- C25 pad 2: DP1_TXD3_HDMI_TXC_N -> GND
- C26 pad 1: DP1_AUX_N -> +3V3
- C26 pad 2: DP1_AUX_HDMI_I2C_SDA_N -> GND
- C27 pad 1: /HDMI/HDMI_D2_P -> /USB Debug, DP/FTDI_3V3
- C27 pad 2: DP1_TXD0_HDMI_TX2_P -> GND
- C28 pad 1: /HDMI/HDMI_D1_P -> /USB Debug, DP/PDC_LDO_1V8
- C28 pad 2: DP1_TXD1_HDMI_TX1_P -> GND
- C29 pad 1: /HDMI/HDMI_D0_P -> /USB Debug, DP/FTDI_3V3
- C29 pad 2: DP1_TXD2_HDMI_TX0_P -> GND
- C3 pad 1: PCIE2_TX0_P -> +1V8
- C3 pad 2: /Peripherals/PCIE2_TX0_CONN_P -> GND
- C30 pad 1: /HDMI/HDMI_CLK_P -> /USB Debug, DP/PDC_LDO_3V3
- C30 pad 2: DP1_TXD3_HDMI_TXC_P -> GND
- C31 pad 1: DP1_TXD0_P -> Net-(C31-Pad1)
- C31 pad 2: DP1_TXD0_HDMI_TX2_P -> GND
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
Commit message: Started placement
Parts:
- removed C40, C41, C42, C43, C44, C48, C49, C50, C51, C52, C83: C_100n_0402, antmicro-footprints:0402-cap
- added D29: DF2S30FS, antmicro-footprints:SOD-923, F.Cu at (-55.1, 45.9)
- added D30: ESD9X5.0ST5G, antmicro-footprints:SOD-923, F.Cu at (31.0, 157.8)
- added D31: ESD9X5.0ST5G, antmicro-footprints:SOD-923, F.Cu at (81.2, 157.7)
- added D32: ESD9X5.0ST5G, antmicro-footprints:SOD-923, F.Cu at (57.9, 186.8)
- added D33: ESD9X5.0ST5G, antmicro-footprints:SOD-923, F.Cu at (58.2, 169.0)
- added U47: RB521S30T1G, antmicro-footprints:SOD-523, F.Cu at (-47.8, 46.1)
- added kibuzzard-633EE390: G***, kibuzzard-633EE390, F.Cu at (31.3, 64.3)
- C1, C13, C14, C15, C16, C17, C18, C19, C2, C20, C21, C22, C23, C24, C25, C27, C29, C31, C4, C5, C76, C77, C78, C80, D10, D12, D13, D14, FB1, FB2, FB3, J7, R141, R142, R143, R144, R145, R146, R147, R148, R149, R150, R151, R152, R153, R19, R211, R212, R213, R214, R46, R56, R57, R58, R59, R80, R81, S1, S2, S3, U11, U22, U5, Y1: moved to B.Cu
- D28: value 1N4148WS -> DF2S30FS; footprint Diode_SMD:D_SOD-323 -> antmicro-footprints:SOD-923
- J11, SW1, U27, U28: moved to F.Cu
- moved S5 285.8 mm to (123.3, 177.9)
- moved J1 278.3 mm to (-137.7, -8.45), turned to 90 degrees
- moved S4 271.2 mm to (114.8, 177.9)
- moved U37 270.5 mm to (114.8, 171.7), turned to -90 degrees
- moved U38 270.4 mm to (122.0, 172.3), turned to 90 degrees
- moved J10 269.0 mm to (172.7, 136.6), turned to 90 degrees
- moved C118 263.9 mm to (117.8, 171.7)
- moved Q17 262.8 mm to (118.2, 173.7)
- moved U26 261.4 mm to (128.9, 197.5), turned to -90 degrees
- moved Q12 258.3 mm to (111.2, 169.3)
- moved R259 257.7 mm to (120.8, 174.7)
- moved C119 257.0 mm to (119.2, 171.2), turned to 90 degrees
- moved C102 255.5 mm to (168.8, 132.2), turned to 90 degrees
- moved U35 254.0 mm to (105.7, 174.8)
- moved R260 252.1 mm to (120.8, 169.9)
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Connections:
- D28 pad 1: /HDMI/5V_HDMI -> Net-(J12-Pad1)
- D28 pad 2: Net-(D28-Pad2) -> GND
- FB4 pad 2: Net-(D28-Pad2) -> Net-(FB4-Pad2)
- R262 pad 2: +5V -> 3V3_STDB
- U10 pad 10: /USB Debug, DP/DP1_TXD0_C_N -> DP1_TXD0_N
- U10 pad 12: /USB Debug, DP/DP1_TXD1_C_P -> DP1_TXD1_P
- U10 pad 13: /USB Debug, DP/DP1_TXD1_C_N -> DP1_TXD1_N
- U10 pad 15: /USB Debug, DP/DP1_TXD2_C_P -> DP1_TXD2_P
- U10 pad 16: /USB Debug, DP/DP1_TXD2_C_N -> DP1_TXD2_N
- U10 pad 18: /USB Debug, DP/DP1_TXD3_C_P -> DP1_TXD3_P
- U10 pad 19: /USB Debug, DP/DP1_TXD3_C_N -> DP1_TXD3_N
- U10 pad 24: /USB Debug, DP/DP1_AUX_C_P -> DP1_AUX_P
- U10 pad 25: /USB Debug, DP/DP1_AUX_C_N -> DP1_AUX_N
- U10 pad 9: /USB Debug, DP/DP1_TXD0_C_P -> DP1_TXD0_P
- U44 pad 10: unconnected-(U44-Pad10) -> /HDMI/HDMI_D1_N
- U44 pad 6: unconnected-(U44-Pad6) -> /HDMI/HDMI_D2_P
- U44 pad 7: unconnected-(U44-Pad7) -> /HDMI/HDMI_D2_N
- U44 pad 9: unconnected-(U44-Pad9) -> /HDMI/HDMI_D1_P
- U45 pad 10: unconnected-(U45-Pad10) -> /HDMI/HDMI_CLK_N
- U45 pad 6: unconnected-(U45-Pad6) -> /HDMI/HDMI_D0_P
- U45 pad 7: unconnected-(U45-Pad7) -> /HDMI/HDMI_D0_N
- U45 pad 9: unconnected-(U45-Pad9) -> /HDMI/HDMI_CLK_P
- U46 pad 10: unconnected-(U46-Pad10) -> /HDMI/HDMI_CEC_5V
- U46 pad 6: unconnected-(U46-Pad6) -> /HDMI/HDMI_SCL_5V
- U46 pad 7: unconnected-(U46-Pad7) -> /HDMI/HDMI_SDA_5V
- U46 pad 9: unconnected-(U46-Pad9) -> /HDMI/HDMI_HPD_5V

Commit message: Finish grouping components
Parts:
- removed R10, R7, R8, R9: R_0R_0402, antmicro-footprints:0402-res
- added D34: RB521S30T1G, antmicro-footprints:SOD-523, B.Cu at (60.4, 61.6)
- added R294: R_2k2_0402, antmicro-footprints:0402-res, B.Cu at (60.8, 62.9)
- BAT1, C64, C65, C84, C85, C86, C94, C95, C98, C99, D18, D20, D24, D25, D6, D7, IC1, R109, R110, R155, R156, R157, R194, R197, R199, R200, R201, R202, R205, R206, R207, R208, R209, R210: moved to B.Cu
- C1, C2, C4, C5, FB1: moved to F.Cu
- C28, C30: value C_10u_0603 -> C_10u_0402; footprint antmicro-footprints:0603-cap -> antmicro-footprints:0402-cap
- J12: value PJ-102A -> 1053131102; footprint antmicro-footprints:Barrel_Jack_5.5mmODx2.1mmID_PJ-102A -> antmicro-footprints:1053131102
- moved TP56 351.5 mm to (-343.2, 34.5), turned to 90 degrees
- moved TP1 348.6 mm to (-343.2, 36.7), turned to 90 degrees
- moved TP5 343.9 mm to (-343.2, 41.2), turned to 90 degrees
- moved TP4 341.0 mm to (-343.2, 43.4), turned to 90 degrees
- moved TP57 340.7 mm to (-343.2, 39.0), turned to 90 degrees
- moved TP3 338.9 mm to (-343.2, 45.7), turned to 90 degrees
- moved TP2 334.0 mm to (-343.2, 47.9), turned to 90 degrees
- moved TP45 315.9 mm to (-343.2, 50.2), turned to 90 degrees
- moved TP41 314.1 mm to (-343.2, 52.4), turned to 90 degrees
- moved TP37 313.6 mm to (-343.2, 54.6), turned to 90 degrees
- moved TP39 310.0 mm to (-343.2, 56.9), turned to 90 degrees
- moved TP30 309.2 mm to (-343.2, 77.1), turned to 90 degrees
- moved TP44 308.6 mm to (-343.2, 59.1), turned to 90 degrees
- moved TP38 305.7 mm to (-343.2, 61.4), turned to 90 degrees
- moved TP33 303.7 mm to (-343.2, 81.5), turned to 90 degrees
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- renumbered U4 to D35, U35 to D36, U36 to D37, U47 to D38
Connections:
- A1 pad 185: Net-(A1-Pad185) -> SYS_SCL
- A1 pad 187: Net-(A1-Pad187) -> SYS_SDA
- A1 pad 189: Net-(A1-Pad189) -> I2C1_SCL
- A1 pad 191: Net-(A1-Pad191) -> I2C1_SDA
- BAT1 pad +: /SoM/PMIC_BBAT -> Net-(BAT1-Pad+)
- R16 pad 2: /M.2/~{M2_M_PERST} -> /M.2/~{M2_M_PEWAKE0}
- R18 pad 2: /M.2/~{M2_M_PEWAKE0} -> /M.2/~{M2_M_PERST}
